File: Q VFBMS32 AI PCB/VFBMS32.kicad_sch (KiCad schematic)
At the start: 9 parts, among them Q1 AGM15T03LL (CHG FET), Q2 AGM15T03LL (DSG FET), U1 BQ7695202 (IC1 - Lower 16S), U2 BQ7695202 (IC2 - Upper 16S), U3 ESP32-C3-MINI-1, U5 SN65HVD230 (CAN Transceiver)

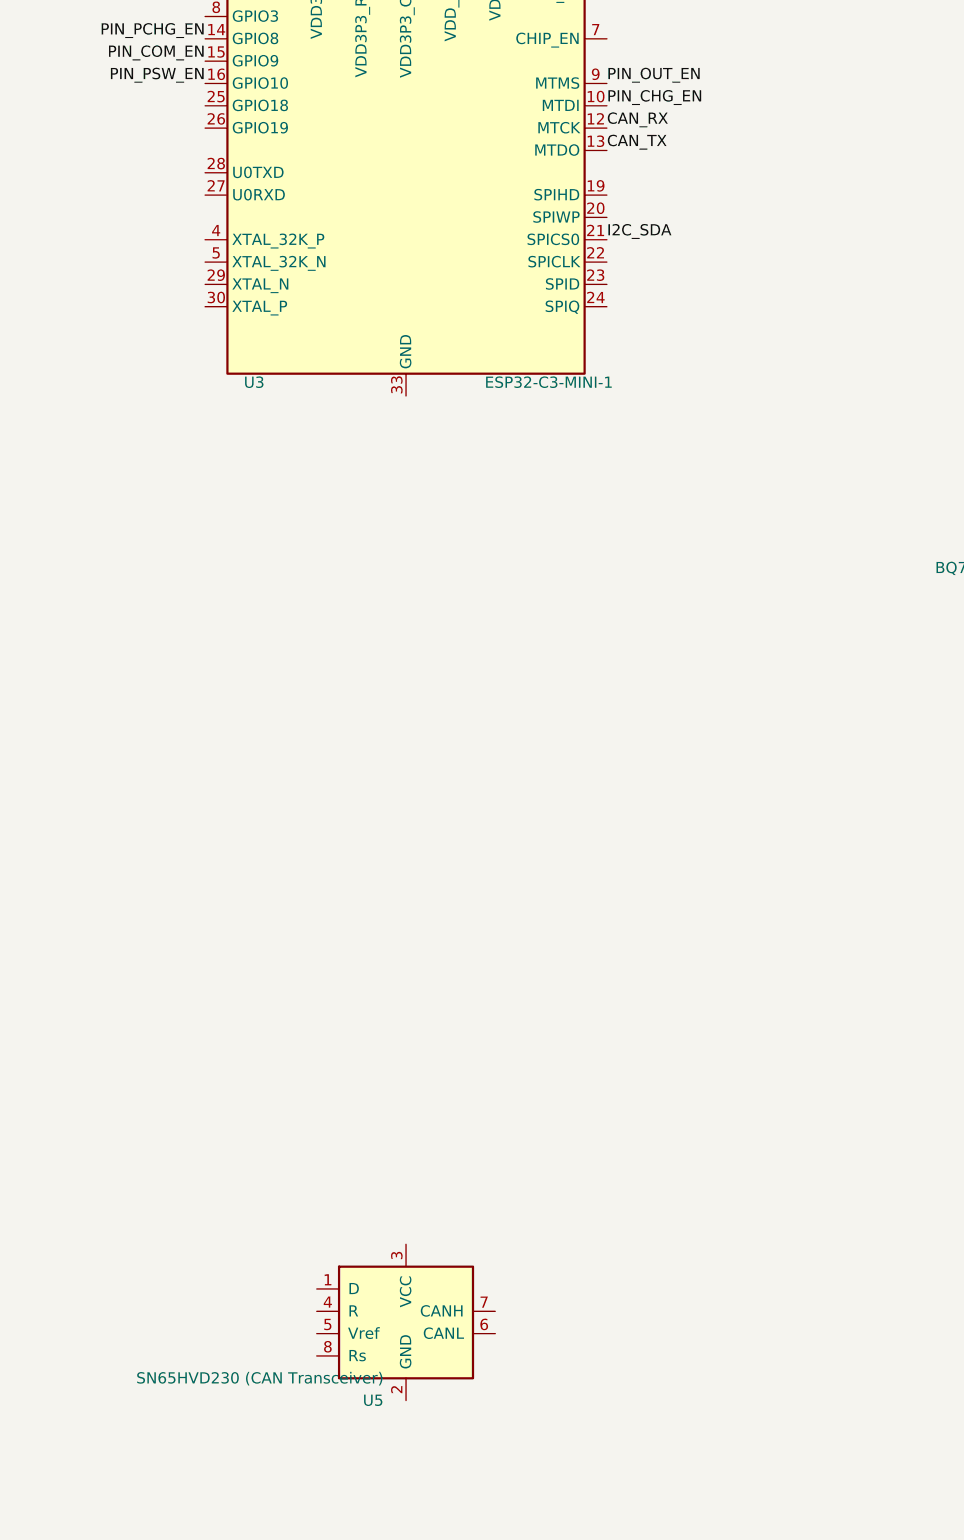
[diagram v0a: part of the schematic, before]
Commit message: feat: add VFBMS32 AI PCB schematic, layout, and supporting automation scripts
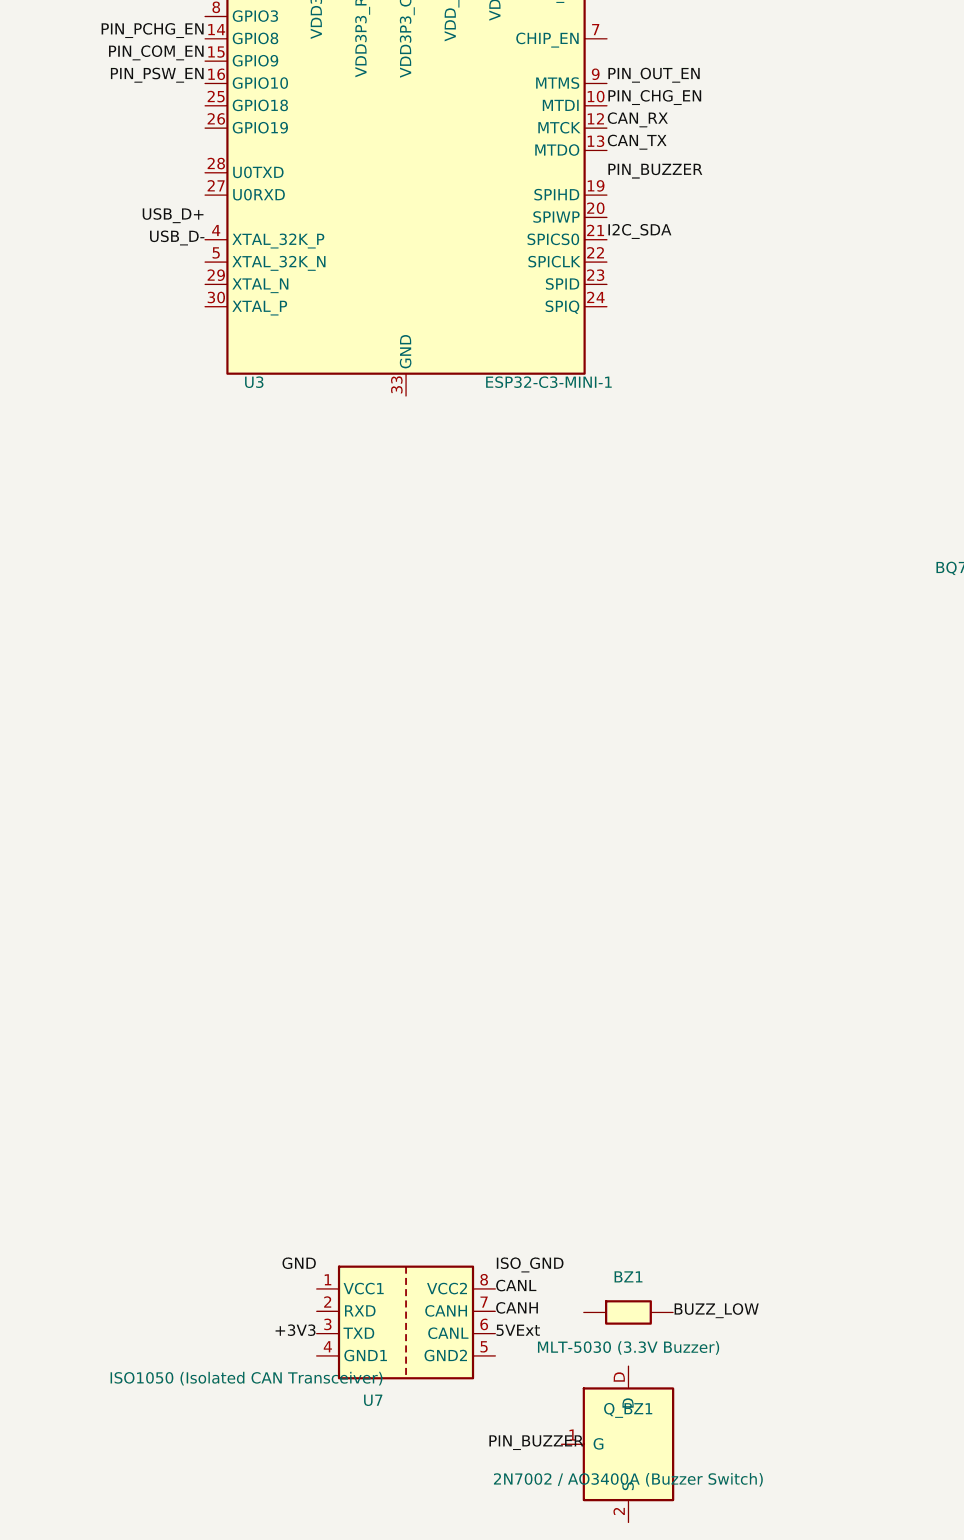
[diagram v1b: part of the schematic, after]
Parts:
- added BZ1: MLT-5030 (3.3V Buzzer), vfbms:Buzzer_5.0x5.0mm_SMD, symbol Device:Buzzer
- added Q_BZ1: 2N7002 / AO3400A (Buzzer Switch), Package_TO_SOT_SMD:SOT-23, symbol vfbms:AGM15T03LL
- U7: renamed from U5; value SN65HVD230 (CAN Transceiver) -> ISO1050 (Isolated CAN Transceiver); footprint Package_SO:SOIC-8_3.9x4.9mm_P1.27mm -> Package_DIP:SMDIP-8_W9.53mm; symbol Interface_CAN_LIN:SN65HVD230 -> Interface_CAN_LIN:ISO1050DUB
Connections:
- net USB_D-: now reaches U3.4 (XTAL_32K_P)
- net +3V3: now reaches U7.3 (TXD)
- net 5VExt: now reaches U7.6 (CANL)
- net CANH: now reaches U7.7 (CANH)
- net CANL: now reaches U7.8 (VCC2)
- new net BUZZ_LOW: BZ1.2 (-)
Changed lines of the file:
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@@
-		)
-	)
-	(symbol
-		(lib_id "Interface_CAN_LIN:SN65HVD230")
-		(at 59.69 229.87 0)
-		(unit 1)
-		(body_style 1)
-		(exclude_from_sim no)
-		(in_bom yes)
-		(on_board yes)
-		(in_pos_files yes)
-		(dnp no)
-		(property "Reference" "U5"
-			(at 57.15 240.03 0)
-			(show_name no)
-			(do_not_autoplace no)
-			(effects
-				(font
-					(size 1.27 1.27)
-				)
-				(justify right)
-			)
-		)
-		(property "Value" "SN65HVD230 (CAN Transceiver)"
-			(at 57.15 237.49 0)
-			(show_name no)
-			(do_not_autoplace no)
-			(effects
-				(font
-					(size 1.27 1.27)
-				)
-				(justify right)
-			)
-		)
-		(property "Footprint" "Package_SO:SOIC-8_3.9x4.9mm_P1.27mm"
-			(at 59.69 217.17 0)
-			(hide yes)
-			(show_name no)
-			(do_not_autoplace no)
-			(effects
-				(font
-					(size 1.27 1.27)
-				)
-			)
-		)
-		(property "Datasheet" "http://www.ti.com/lit/ds/symlink/sn65hvd230.pdf"
-			(at 57.15 240.03 0)
-			(hide yes)
-			(show_name no)
-			(do_not_autoplace no)
-			(effects
-				(font
-					(size 1.27 1.27)
-				)
-			)
-		)
-		(property "Description" "CAN Bus Transceivers, 3.3V, 1Mbps, Low-Power capabilities, SOIC-8"
-			(at 59.69 229.87 0)
-			(hide yes)
-			(show_name no)
-			(do_not_autoplace no)
-			(effects
-				(font
-					(size 1.27 1.27)
-				)
-			)
-		)
-		(pin "1"
-		)
-		(pin "2"
-		)
-		(pin "3"
-		)
-		(pin "4"
-		)
-		(pin "5"
-		)
-		(pin "6"
-		)
-		(pin "7"
-		)
-		(pin "8"
-		)
-		(instances
-			(project "VFBMS32"
-				(path "/a2322edc-ff52-449c-92df-24faffac0236"
-					(reference "U5")
-					(unit 1)
-				)
-			)
 		)
 	)
@@
 		)
 	)
+	(symbol
+		(lib_id "Interface_CAN_LIN:ISO1050DUB")
+		(at 59.69 229.87 0)
+		(unit 1)
+		(body_style 1)
+		(exclude_from_sim no)
+		(in_bom yes)
+		(on_board yes)
+		(in_pos_files yes)
+		(dnp no)
+		(property "Reference" "U7"
+			(at 57.15 240.03 0)
+			(show_name no)
+			(do_not_autoplace no)
+			(effects
+				(font
+					(size 1.27 1.27)
+				)
+				(justify right)
+			)
+		)
+		(property "Value" "ISO1050 (Isolated CAN Transceiver)"
+			(at 57.15 237.49 0)
+			(show_name no)
+			(do_not_autoplace no)
+			(effects
+				(font
+					(size 1.27 1.27)
+				)
+				(justify right)
+			)
+		)
+		(property "Footprint" "Package_DIP:SMDIP-8_W9.53mm"
+			(at 59.69 217.17 0)
+			(hide yes)
+			(show_name no)
+			(do_not_autoplace no)
+			(effects
+				(font
+					(size 1.27 1.27)
+				)
+			)
+		)
+		(property "Datasheet" "http://www.ti.com/lit/ds/symlink/iso1050.pdf"
+			(at 57.15 240.03 0)
+			(hide yes)
+			(show_name no)
+			(do_not_autoplace no)
+			(effects
+				(font
+					(size 1.27 1.27)
+				)
+			)
+		)
+		(property "Description" "Isolated 5V CAN Transceiver, SOIC-8 Wide"
+			(at 59.69 229.87 0)
+			(hide yes)
+			(show_name no)
+			(do_not_autoplace no)
+			(effects
+				(font
+					(size 1.27 1.27)
+				)
+			)
+		)
+		(pin "1" (uuid "u7-pin-1"))
+		(pin "2" (uuid "u7-pin-2"))
+		(pin "3" (uuid "u7-pin-3"))
+		(pin "4" (uuid "u7-pin-4"))
+		(pin "5" (uuid "u7-pin-5"))
+		(pin "6" (uuid "u7-pin-6"))
+		(pin "7" (uuid "u7-pin-7"))
+		(pin "8" (uuid "u7-pin-8"))
+		(instances
+			(project "VFBMS32"
+				(path "/a2322edc-ff52-449c-92df-24faffac0236"
+					(reference "U7")
+					(unit 1)
+				)
+			)
+		)
+	)
+	(label "USB_D-" (at 36.83 107.95 180) (fields_autoplaced yes) (effects (font (size 1.27 1.27)) (justify right)) (uuid "usb-dm-label"))
+	(label "USB_D+" (at 36.83 105.41 180) (fields_autoplaced yes) (effects (font (size 1.27 1.27)) (justify right)) (uuid "usb-dp-label"))
+	(label "5VExt" (at 69.85 232.41 0) (fields_autoplaced yes) (effects (font (size 1.27 1.27)) (justify left)) (uuid "5vext-label"))
+	(label "ISO_GND" (at 69.85 224.79 0) (fields_autoplaced yes) (effects (font (size 1.27 1.27)) (justify left)) (uuid "isognd-label"))
+	(label "CANH" (at 69.85 229.87 0) (fields_autoplaced yes) (effects (font (size 1.27 1.27)) (justify left)) (uuid "canh-label"))
+	(label "CANL" (at 69.85 227.33 0) (fields_autoplaced yes) (effects (font (size 1.27 1.27)) (justify left)) (uuid "canl-label"))
+	(label "+3V3" (at 49.53 232.41 180) (fields_autoplaced yes) (effects (font (size 1.27 1.27)) (justify right)) (uuid "vcc1-label"))
+	(label "GND" (at 49.53 224.79 180) (fields_autoplaced yes) (effects (font (size 1.27 1.27)) (justify right)) (uuid "gnd1-label"))
+	(symbol
+		(lib_id "Device:Buzzer")
+		(at 85.0 230.0 0)
+		(unit 1)
+		(property "Reference" "BZ1"
+			(at 85.0 226.0 0)
+			(effects (font (size 1.27 1.27)))
+		)
+		(property "Value" "MLT-5030 (3.3V Buzzer)"
+			(at 85.0 234.0 0)
+			(effects (font (size 1.27 1.27)))
+		)
+		(property "Footprint" "vfbms:Buzzer_5.0x5.0mm_SMD"
+			(at 85.0 230.0 0)
+			(hide yes)
+			(effects (font (size 1.27 1.27)))
+		)
+		(pin "1" (uuid "bz1-p1"))
+		(pin "2" (uuid "bz1-p2"))
+		(instances
+			(project "VFBMS32"
+				(path "/a2322edc-ff52-449c-92df-24faffac0236"
+					(reference "BZ1")
+					(unit 1)
+				)
+			)
+		)
+	)
+	(symbol
+		(lib_id "vfbms:AGM15T03LL")
+		(at 85.0 245.0 0)
+		(unit 1)
+		(property "Reference" "Q_BZ1"
+			(at 85.0 241.0 0)
+			(effects (font (size 1.27 1.27)))
+		)
+		(property "Value" "2N7002 / AO3400A (Buzzer Switch)"
+			(at 85.0 249.0 0)
+			(effects (font (size 1.27 1.27)))
+		)
+		(property "Footprint" "Package_TO_SOT_SMD:SOT-23"
+			(at 85.0 245.0 0)
+			(hide yes)
+			(effects (font (size 1.27 1.27)))
+		)
+		(pin "1" (uuid "qbz-p1"))
+		(pin "2" (uuid "qbz-p2"))
+		(pin "3" (uuid "qbz-p3"))
+		(instances
+			(project "VFBMS32"
+				(path "/a2322edc-ff52-449c-92df-24faffac0236"
+					(reference "Q_BZ1")
+					(unit 1)
+				)
+			)
+		)
+	)
+	(label "PIN_BUZZER" (at 82.55 100.33 0) (fields_autoplaced yes) (effects (font (size 1.27 1.27)) (justify left)) (uuid "buzzer-gpio3-label"))
+	(label "BUZZ_LOW" (at 90.08 230.0 0) (fields_autoplaced yes) (effects (font (size 1.27 1.27)) (justify left)) (uuid "bz-low-label"))
+	(label "PIN_BUZZER" (at 79.92 245.0 180) (fields_autoplaced yes) (effects (font (size 1.27 1.27)) (justify right)) (uuid "bz-gate-label"))
 )

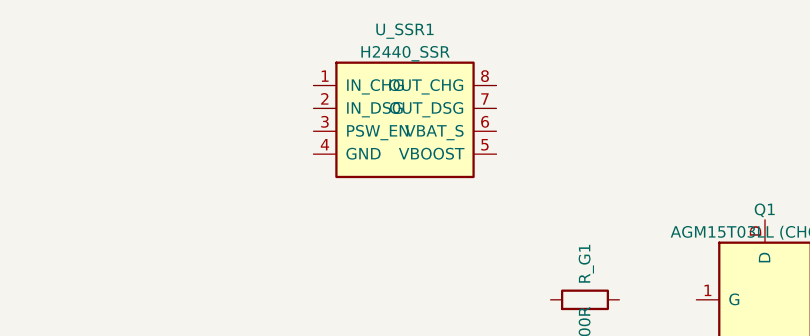
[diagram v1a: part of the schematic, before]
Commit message: feat: add new KiCad PCB designs and layouts for sf hall ai pcb and Q VFBMS32 AI PCB
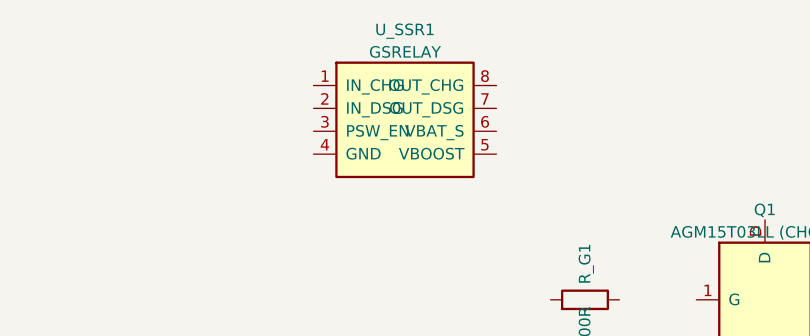
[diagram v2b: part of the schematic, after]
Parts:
- U_SSR1: value H2440_SSR -> GSRELAY; footprint Package_SO:SOIC-8_3.9x4.9mm_P1.27mm -> Package_SO:SOIC-8_7.5x5.85mm_P1.27mm
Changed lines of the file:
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@@
 		(dnp no)
 		(property "Reference" "U_SSR1" (at 155.0 15.0 0) (effects (font (size 1.27 1.27))))
-		(property "Value" "H2440_SSR" (at 155.0 17.5 0) (effects (font (size 1.27 1.27))))
-		(property "Footprint" "Package_SO:SOIC-8_3.9x4.9mm_P1.27mm" (at 155.0 13.0 0) (hide yes) (effects (font (size 1.27 1.27))))
+		(property "Value" "GSRELAY" (at 155.0 17.5 0) (effects (font (size 1.27 1.27))))
+		(property "Footprint" "Package_SO:SOIC-8_7.5x5.85mm_P1.27mm" (at 155.0 13.0 0) (hide yes) (effects (font (size 1.27 1.27))))
 		(pin "1")
 		(pin "2")

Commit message: feat: add PCB layout project, KiCad bridge, dashboard, and annotator toolset
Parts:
- added D: D_Schottky
- added D_CHG1, D_CHG2, D_CHG3: DSK320, Diode_SMD:D_SOD-123F, symbol Device:D_Schottky
- added R_CHG1: 100k, Resistor_SMD:R_0603_1608Metric, symbol Device:R
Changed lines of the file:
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@@
 		(effects (font (size 1.27 1.27)) (justify left bottom))
+	)
+		(symbol "Device:D_Schottky"
+		(pin_numbers
+			(hide yes)
+		)
+		(pin_names
+			(offset 1.016)
+			(hide yes)
+		)
+		(exclude_from_sim no)
+		(in_bom yes)
+		(on_board yes)
+		(in_pos_files yes)
+		(duplicate_pin_numbers_are_jumpers no)
+		(property "Reference" "D"
+			(at 0 2.54 0)
+			(show_name no)
+			(do_not_autoplace no)
+			(effects
+				(font
+					(size 1.27 1.27)
+				)
+			)
+		)
+		(property "Value" "D_Schottky"
+			(at 0 -2.54 0)
+			(show_name no)
+			(do_not_autoplace no)
+			(effects
+				(font
+					(size 1.27 1.27)
+				)
+			)
+		)
+		(property "Footprint" ""
+			(at 0 0 0)
+			(show_name no)
+			(do_not_autoplace no)
+			(hide yes)
+			(effects
+				(font
+					(size 1.27 1.27)
+				)
+			)
+		)
+		(property "Datasheet" ""
+			(at 0 0 0)
+			(show_name no)
+			(do_not_autoplace no)
+			(hide yes)
+			(effects
+				(font
+					(size 1.27 1.27)
+				)
+			)
+		)
+		(property "Description" "Schottky diode"
+			(at 0 0 0)
+			(show_name no)
+			(do_not_autoplace no)
+			(hide yes)
+			(effects
+				(font
+					(size 1.27 1.27)
+				)
+			)
+		)
+		(property "ki_keywords" "diode Schottky"
+			(at 0 0 0)
+			(show_name no)
+			(do_not_autoplace no)
+			(hide yes)
+			(effects
+				(font
+					(size 1.27 1.27)
+				)
+			)
+		)
+		(property "ki_fp_filters" "TO-???* *_Diode_* *SingleDiode* D_*"
+			(at 0 0 0)
+			(show_name no)
+			(do_not_autoplace no)
+			(hide yes)
+			(effects
+				(font
+					(size 1.27 1.27)
+				)
+			)
+		)
+		(symbol "D_Schottky_0_1"
+			(polyline
+				(pts
+					(xy -1.905 0.635) (xy -1.905 1.27) (xy -1.27 1.27) (xy -1.27 -1.27) (xy -0.635 -1.27) (xy -0.635 -0.635)
+				)
+				(stroke
+					(width 0.254)
+					(type default)
+				)
+				(fill
+					(type none)
+				)
+			)
+			(polyline
+				(pts
+					(xy 1.27 1.27) (xy 1.27 -1.27) (xy -1.27 0) (xy 1.27 1.27)
+				)
+				(stroke
+					(width 0.254)
+					(type default)
+				)
+				(fill
+					(type none)
+				)
+			)
+			(polyline
+				(pts
+					(xy 1.27 0) (xy -1.27 0)
+				)
+				(stroke
+					(width 0)
+					(type default)
+				)
+				(fill
+					(type none)
+				)
+			)
+		)
+		(symbol "D_Schottky_1_1"
+			(pin passive line
+				(at -3.81 0 0)
+				(length 2.54)
+				(name "K"
+					(effects
+						(font
+							(size 1.27 1.27)
+						)
+					)
+				)
+				(number "1"
+					(effects
+						(font
+							(size 1.27 1.27)
+						)
+					)
+				)
+			)
+			(pin passive line
+				(at 3.81 0 180)
+				(length 2.54)
+				(name "A"
+					(effects
+						(font
+							(size 1.27 1.27)
+						)
+					)
+				)
+				(number "2"
+					(effects
+						(font
+							(size 1.27 1.27)
+						)
+					)
+				)
+			)
+		)
+		(embedded_fonts no)
+	)
+	(symbol (lib_id "Device:R")
+		(at 175.0 105.0 0)
+		(unit 1)
+		(exclude_from_sim no)
+		(in_bom yes)
+		(on_board yes)
+		(dnp no)
+		(property "Reference" "R_CHG1" (at 175.0 101.0 0) (effects (font (size 1.27 1.27))))
+		(property "Value" "100k" (at 175.0 109.0 0) (effects (font (size 1.27 1.27))))
+		(property "Footprint" "Resistor_SMD:R_0603_1608Metric" (at 175.0 105.0 0) (hide yes) (effects (font (size 1.27 1.27))))
+		(pin "1")
+		(pin "2")
+		(instances
+			(project "VFBMS32"
+				(path "/a2322edc-ff52-449c-92df-24faffac0236" (reference "R_CHG1") (unit 1))
+			)
+		)
+	)
+	(symbol (lib_id "Device:D_Schottky")
+		(at 195.0 105.0 0)
+		(unit 1)
+		(exclude_from_sim no)
+		(in_bom yes)
+		(on_board yes)
+		(dnp no)
+		(property "Reference" "D_CHG1" (at 195.0 101.0 0) (effects (font (size 1.27 1.27))))
+		(property "Value" "DSK320" (at 195.0 109.0 0) (effects (font (size 1.27 1.27))))
+		(property "Footprint" "Diode_SMD:D_SOD-123F" (at 195.0 105.0 0) (hide yes) (effects (font (size 1.27 1.27))))
+		(pin "1")
+		(pin "2")
+		(instances
+			(project "VFBMS32"
+				(path "/a2322edc-ff52-449c-92df-24faffac0236" (reference "D_CHG1") (unit 1))
+			)
+		)
+	)
+	(symbol (lib_id "Device:D_Schottky")
+		(at 205.0 105.0 0)
+		(unit 1)
+		(exclude_from_sim no)
+		(in_bom yes)
+		(on_board yes)
+		(dnp no)
+		(property "Reference" "D_CHG2" (at 205.0 101.0 0) (effects (font (size 1.27 1.27))))
+		(property "Value" "DSK320" (at 205.0 109.0 0) (effects (font (size 1.27 1.27))))
+		(property "Footprint" "Diode_SMD:D_SOD-123F" (at 205.0 105.0 0) (hide yes) (effects (font (size 1.27 1.27))))
+		(pin "1")
+		(pin "2")
+		(instances
+			(project "VFBMS32"
+				(path "/a2322edc-ff52-449c-92df-24faffac0236" (reference "D_CHG2") (unit 1))
+			)
+		)
+	)
+	(symbol (lib_id "Device:D_Schottky")
+		(at 215.0 105.0 0)
+		(unit 1)
+		(exclude_from_sim no)
+		(in_bom yes)
+		(on_board yes)
+		(dnp no)
+		(property "Reference" "D_CHG3" (at 215.0 101.0 0) (effects (font (size 1.27 1.27))))
+		(property "Value" "DSK320" (at 215.0 109.0 0) (effects (font (size 1.27 1.27))))
+		(property "Footprint" "Diode_SMD:D_SOD-123F" (at 215.0 105.0 0) (hide yes) (effects (font (size 1.27 1.27))))
+		(pin "1")
+		(pin "2")
+		(instances
+			(project "VFBMS32"
+				(path "/a2322edc-ff52-449c-92df-24faffac0236" (reference "D_CHG3") (unit 1))
+			)
+		)
 	)
 	(sheet_instances

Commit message: remove  old bad work vfbms  AI PCB
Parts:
- added C_FLT1: 10uF_100V, Capacitor_SMD:C_1812_4532Metric, symbol Device:C
- added R_B33: 27R0, Resistor_SMD:R_0805_2012Metric, symbol Device:R
- U_SSR1: footprint Package_SO:SOIC-8_7.5x5.85mm_P1.27mm -> vfbms:H2440_SSR
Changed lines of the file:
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@@
 		(property "Reference" "U_SSR1" (at 155.0 15.0 0) (effects (font (size 1.27 1.27))))
 		(property "Value" "GSRELAY" (at 155.0 17.5 0) (effects (font (size 1.27 1.27))))
-		(property "Footprint" "Package_SO:SOIC-8_7.5x5.85mm_P1.27mm" (at 155.0 13.0 0) (hide yes) (effects (font (size 1.27 1.27))))
+		(property "Footprint" "vfbms:H2440_SSR" (at 155.0 13.0 0) (hide yes) (effects (font (size 1.27 1.27))))
 		(pin "1")
 		(pin "2")
@@
 			)
 		)
+	)
+	(symbol (lib_id "Device:C")
+		(at 225.0 105.0 0)
+		(unit 1)
+		(exclude_from_sim no)
+		(in_bom yes)
+		(on_board yes)
+		(dnp no)
+		(property "Reference" "C_FLT1" (at 225.0 101.0 0) (effects (font (size 1.27 1.27))))
+		(property "Value" "10uF_100V" (at 225.0 109.0 0) (effects (font (size 1.27 1.27))))
+		(property "Footprint" "Capacitor_SMD:C_1812_4532Metric" (at 225.0 105.0 0) (hide yes) (effects (font (size 1.27 1.27))))
+		(pin "1")
+		(pin "2")
+		(instances
+			(project "VFBMS32"
+				(path "/a2322edc-ff52-449c-92df-24faffac0236" (reference "C_FLT1") (unit 1))
+			)
+		)
+	)
+	(symbol (lib_id "Device:R")
+		(at 235.0 105.0 0)
+		(unit 1)
+		(exclude_from_sim no)
+		(in_bom yes)
+		(on_board yes)
+		(dnp no)
+		(property "Reference" "R_B33" (at 235.0 101.0 0) (effects (font (size 1.27 1.27))))
+		(property "Value" "27R0" (at 235.0 109.0 0) (effects (font (size 1.27 1.27))))
+		(property "Footprint" "Resistor_SMD:R_0805_2012Metric" (at 235.0 105.0 0) (hide yes) (effects (font (size 1.27 1.27))))
+		(pin "1")
+		(pin "2")
+		(instances
+			(project "VFBMS32"
+				(path "/a2322edc-ff52-449c-92df-24faffac0236" (reference "R_B33") (unit 1))
+			)
+		)
